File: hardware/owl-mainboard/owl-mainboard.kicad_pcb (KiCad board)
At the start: 4 copper layers, 61.8 x 79.8 mm, 106 parts, among them J101 Battery +, NTC, -, J201 USB-C, J202 EXP: GND, 3V3, A, B, J301 AMOLED FPC, J302 LRA, J303 DOCK: GND, VBUS, DET, GND, SW201 Ear left, SW202 Ear right, SW203 Beak, U101 BQ24073RGTR, U102 MAX17048G+T10, U103 TPS63802DLAR, U104 TPS22917DBVR, U201 ESP32-S3-WROOM-1-N16R8, U202 USBLC6-2SC6, U301 DRV2605LDGSR, U302 TMAG5273A2QDBVR, U303 LIS2DW12TR, U304 OPT3001DNPR, Y201 32.768kHz 12.5pF

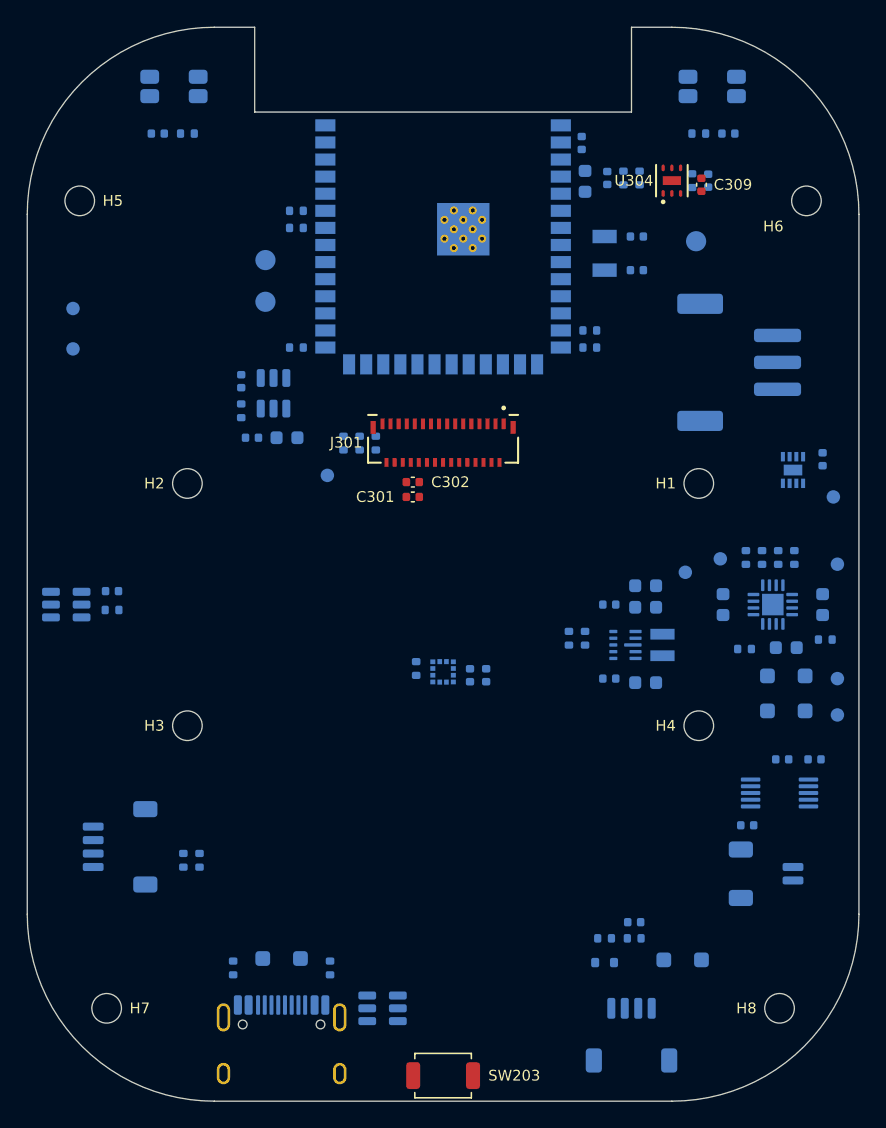
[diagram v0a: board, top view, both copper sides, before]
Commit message: fix(hardware): straighten the USB pair, move C304 and C106 to their pins, put the holes on the front
R203 and R204 stand below U201 pins 14 and 13 with their connector pads at the bottom, and U202
turns to 180 so D+ runs above D- on both sides: the pair goes from J201 through U202 to U201
without crossing (0 crossing airwires). C304 spans DRV2605L VDD pin 10 and GND pin 8, C106 sits
at TPS63802 VIN pin 10 with C105 behind it, and L101's courtyard leaves the battery zone (R44).
H1 to H8 are front in design.toml, as on the board (a bare hole has no side), and the side test
covers them. mark_j101 removes only its own pin 1 dot. R102 3.6k synced from the schematic.
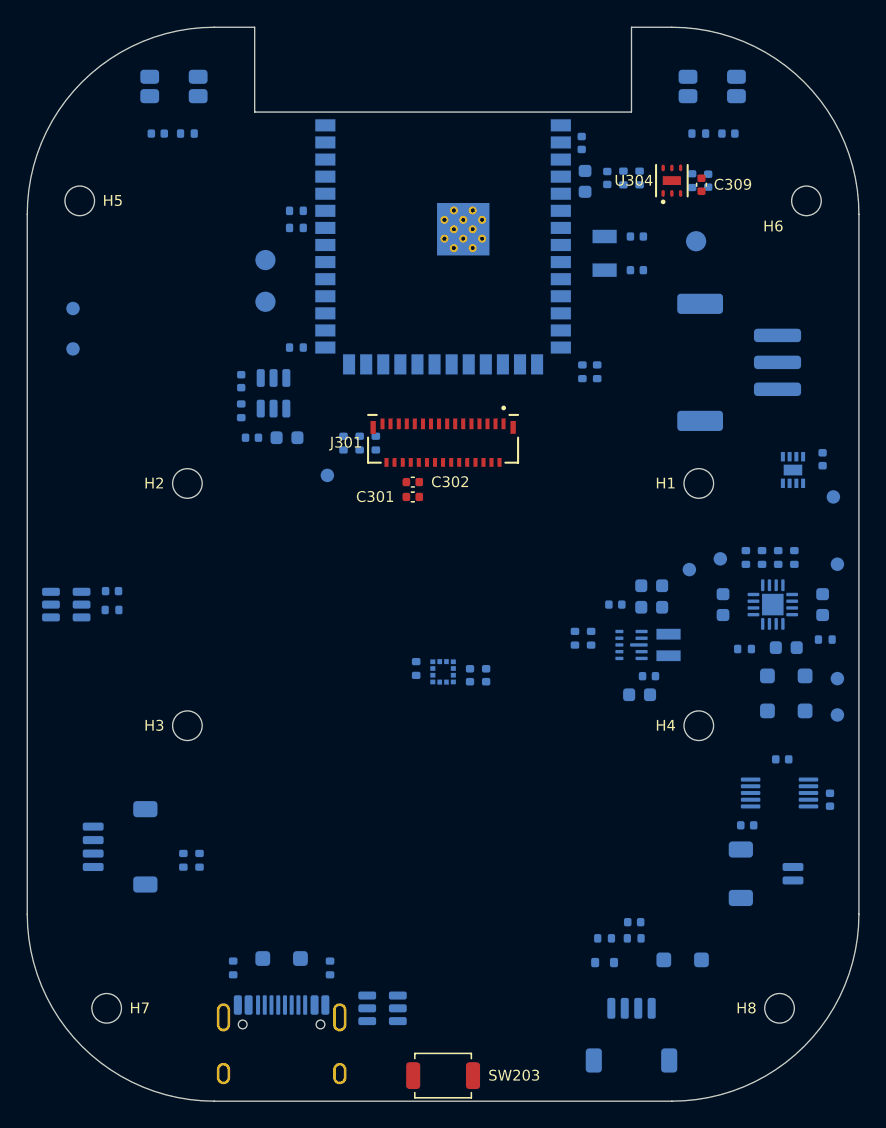
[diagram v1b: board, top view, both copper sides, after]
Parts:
- R102: value 3.3k -> 3.6k
- moved C304 3.21 mm to (128.8, 114.5), turned to 90 degrees
- moved R204 3.12 mm to (111.5, 82.7), turned to 90 degrees
- moved C106 2.96 mm to (115.3, 105.3)
- moved R203 1.88 mm to (110.3, 82.7), turned to 90 degrees
- moved C105 1.01 mm to (114.6, 106.7)
- moved C107 0.45 mm to (115.5, 100.2)
- moved C108 0.45 mm to (115.5, 98.6)
- moved C109 0.45 mm to (112.8, 100.0)
- moved L101 0.45 mm to (116.8, 103.0)
- moved R107 0.45 mm to (111.0, 102.5)
- moved R108 0.45 mm to (109.8, 102.5)
- moved U103 0.45 mm to (114.0, 103.0)
- moved TP104 0.36 mm to (118.3, 97.4)
- turned U202 to 180 degrees

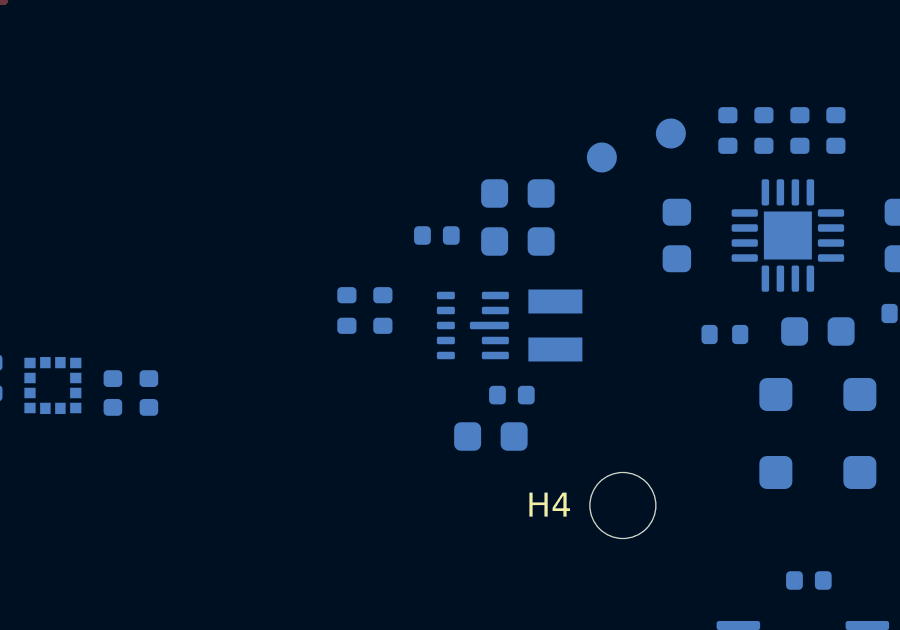
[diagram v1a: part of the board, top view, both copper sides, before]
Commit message: feat(hardware): route the TPS63802 power loop
tools/hw/hw_route.py draws the hand-routed groups as locked B.Cu tracks. The TPS63802 group: L1
and L2 at 0.5 mm straight into L101 (necked to 0.3 mm at the 0.5 mm pitch pins, entering the
inductor pads clear of its no-track area), VIN from pin 10 through C106 to C105 at 0.5 mm, EN to
VIN below the package, VOUT from pin 6 through C107 to C108 at 0.5 mm, C109 and the top of the
feedback divider from C107, FB from pin 4 to R107 and R108 on the side away from L1 and L2 (R107
turned so its FB pad faces R108), GND pins 2, 3 and 8 joined between the pad rows. GND vias and
the In1 tie come with the planes. DRC: no new violation type, 272 to 259 unconnected.
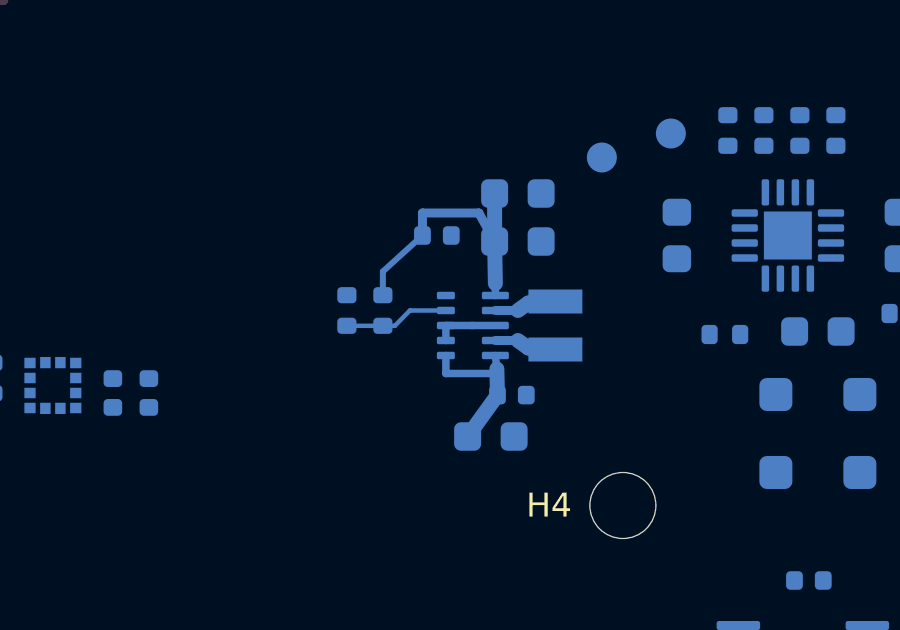
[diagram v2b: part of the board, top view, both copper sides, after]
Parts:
- turned R107 to -90 degrees
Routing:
- net +3V3: track 0.00 -> 9.69 mm
- net VSYS: track 0.00 -> 5.32 mm
- net TPS_FB: track 0.00 -> 3.51 mm
- net TPS_L2: track 0.00 -> 1.83 mm
- net TPS_L1: track 0.00 -> 1.83 mm
- net GND: track 0.00 -> 1.40 mm
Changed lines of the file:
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@@
 	(footprint "Resistor_SMD:R_0402_1005Metric"
 		(layer "B.Cu")
-		(at 111 102.5 90)
+		(at 111 102.5 -90)
 		(descr "Resistor SMD 0402 (1005 Metric), square (rectangular) end terminal, IPC-7351 nominal, (Body size source: IPC-SM-782 page 72, https://www.pcb-3d.com/wordpress/wp-content/uploads/ipc-sm-782a_amendment_1_and_2.pdf)")
 		(tags "resistor")
@@
 		)
 		(property "Value" "560k"
-			(at 0 -1.17 270)
+			(at 0 -1.17 90)
 			(layer "B.Fab")
 			(effects
@@
 		)
 		(property "Datasheet" ""
-			(at 0 0 270)
+			(at 0 0 90)
 			(layer "B.Fab")
 			(hide yes)
@@
 		)
 		(property "Description" "Resistor"
-			(at 0 0 270)
+			(at 0 0 90)
 			(layer "B.Fab")
 			(hide yes)
@@
 		)
 		(property "KiLib_Generator" "SMD_2terminal_chip_molded"
-			(at 0 0 270)
+			(at 0 0 90)
 			(layer "B.SilkS")
 			(hide yes)
@@
 		)
 		(property "LCSC Part #" "C132339"
-			(at 0 0 270)
+			(at 0 0 90)
 			(layer "B.SilkS")
 			(hide yes)
@@
 		)
 		(property "MPN" "0402WGF5603TCE"
-			(at 0 0 270)
+			(at 0 0 90)
 			(layer "B.SilkS")
 			(hide yes)
@@
 		)
 		(property "Manufacturer" "UNI-ROYAL"
-			(at 0 0 270)
+			(at 0 0 90)
 			(layer "B.SilkS")
 			(hide yes)
@@
 		(duplicate_pad_numbers_are_jumpers no)
 		(fp_line
-			(start -0.153641 -0.38)
-			(end 0.153641 -0.38)
+			(start -0.153641 0.38)
+			(end 0.153641 0.38)
 			(stroke
 				(width 0.12)
@@
 		)
 		(fp_line
-			(start -0.153641 0.38)
-			(end 0.153641 0.38)
+			(start -0.153641 -0.38)
+			(end 0.153641 -0.38)
 			(stroke
 				(width 0.12)
@@
 		)
 		(fp_text user "${REFERENCE}"
-			(at 0 0 270)
+			(at 0 0 90)
 			(layer "B.Fab")
 			(effects
@@
 		)
 		(pad "1" smd roundrect
-			(at -0.51 0 90)
+			(at -0.51 0 270)
 			(size 0.54 0.64)
 			(layers "B.Cu" "B.Mask" "B.Paste")
@@
 		)
 		(pad "2" smd roundrect
-			(at 0.51 0 90)
+			(at 0.51 0 270)
 			(size 0.54 0.64)
 			(layers "B.Cu" "B.Mask" "B.Paste")
@@
 		)
 	)
+	(segment
+		(start 113.1 103)
+		(end 114 103)
+		(width 0.25)
+		(locked yes)
+		(layer "B.Cu")
+		(net "GND")
+	)
+	(segment
+		(start 113.1 103.5)
+		(end 113.1 103)
+		(width 0.25)
+		(locked yes)
+		(layer "B.Cu")
+		(net "GND")
+	)
+	(segment
+		(start 112.32 99.25)
+		(end 112.32 100)
+		(width 0.3)
+		(locked yes)
+		(layer "B.Cu")
+		(net "+3V3")
+	)
+	(segment
+		(start 114.75 101.6)
+		(end 114.725 100.2)
+		(width 0.5)
+		(locked yes)
+		(layer "B.Cu")
+		(net "+3V3")
+	)
+	(segment
+		(start 114.725 100.2)
+		(end 114.725 98.6)
+		(width 0.5)
+		(locked yes)
+		(layer "B.Cu")
+		(net "+3V3")
+	)
+	(segment
+		(start 111 101.2)
+		(end 111 101.99)
+		(width 0.2)
+		(locked yes)
+		(layer "B.Cu")
+		(net "+3V3")
+	)
+	(segment
+		(start 114.725 100.2)
+		(end 114.2 99.25)
+		(width 0.3)
+		(locked yes)
+		(layer "B.Cu")
+		(net "+3V3")
+	)
+	(segment
+		(start 114.75 102)
+		(end 114.75 101.6)
+		(width 0.25)
+		(locked yes)
+		(layer "B.Cu")
+		(net "+3V3")
+	)
+	(segment
+		(start 112.32 100)
+		(end 111 101.2)
+		(width 0.2)
+		(locked yes)
+		(layer "B.Cu")
+		(net "+3V3")
+	)
+	(segment
+		(start 114.2 99.25)
+		(end 112.32 99.25)
+		(width 0.3)
+		(locked yes)
+		(layer "B.Cu")
+		(net "+3V3")
+	)
+	(segment
+		(start 114.75 104)
+		(end 114.8 104.45)
+		(width 0.25)
+		(locked yes)
+		(layer "B.Cu")
+		(net "VSYS")
+	)
+	(segment
+		(start 113.1 104)
+		(end 113.1 104.6)
+		(width 0.25)
+		(locked yes)
+		(layer "B.Cu")
+		(net "VSYS")
+	)
+	(segment
+		(start 114.8 104.45)
+		(end 114.82 105.32)
+		(width 0.5)
+		(locked yes)
+		(layer "B.Cu")
+		(net "VSYS")
+	)
+	(segment
+		(start 113.1 104.6)
+		(end 114.8 104.6)
+		(width 0.25)
+		(locked yes)
+		(layer "B.Cu")
+		(net "VSYS")
+	)
+	(segment
+		(start 114.82 105.32)
+		(end 113.825 106.7)
+		(width 0.5)
+		(locked yes)
+		(layer "B.Cu")
+		(net "VSYS")
+	)
+	(segment
+		(start 111.9 102.5)
+		(end 111.4 103.01)
+		(width 0.15)
+		(locked yes)
+		(layer "B.Cu")
+		(net "TPS_FB")
+	)
+	(segment
+		(start 111.4 103.01)
+		(end 111 103.01)
+		(width 0.15)
+		(locked yes)
+		(layer "B.Cu")
+		(net "TPS_FB")
+	)
+	(segment
+		(start 111 103.01)
+		(end 109.8 103.01)
+		(width 0.15)
+		(locked yes)
+		(layer "B.Cu")
+		(net "TPS_FB")
+	)
+	(segment
+		(start 113.1 102.5)
+		(end 111.9 102.5)
+		(width 0.15)
+		(locked yes)
+		(layer "B.Cu")
+		(net "TPS_FB")
+	)
+	(segment
+		(start 115.5 102.5)
+		(end 115.85 102.25)
+		(width 0.5)
+		(locked yes)
+		(layer "B.Cu")
+		(net "TPS_L2")
+	)
+	(segment
+		(start 115.85 102.25)
+		(end 116.5 102.25)
+		(width 0.5)
+		(locked yes)
+		(layer "B.Cu")
+		(net "TPS_L2")
+	)
+	(segment
+		(start 114.75 102.5)
+		(end 115.5 102.5)
+		(width 0.3)
+		(locked yes)
+		(layer "B.Cu")
+		(net "TPS_L2")
+	)
+	(segment
+		(start 115.5 103.5)
+		(end 115.85 103.75)
+		(width 0.5)
+		(locked yes)
+		(layer "B.Cu")
+		(net "TPS_L1")
+	)
+	(segment
+		(start 115.85 103.75)
+		(end 116.5 103.75)
+		(width 0.5)
+		(locked yes)
+		(layer "B.Cu")
+		(net "TPS_L1")
+	)
+	(segment
+		(start 114.75 103.5)
+		(end 115.5 103.5)
+		(width 0.3)
+		(locked yes)
+		(layer "B.Cu")
+		(net "TPS_L1")
+	)
 	(embedded_fonts no)

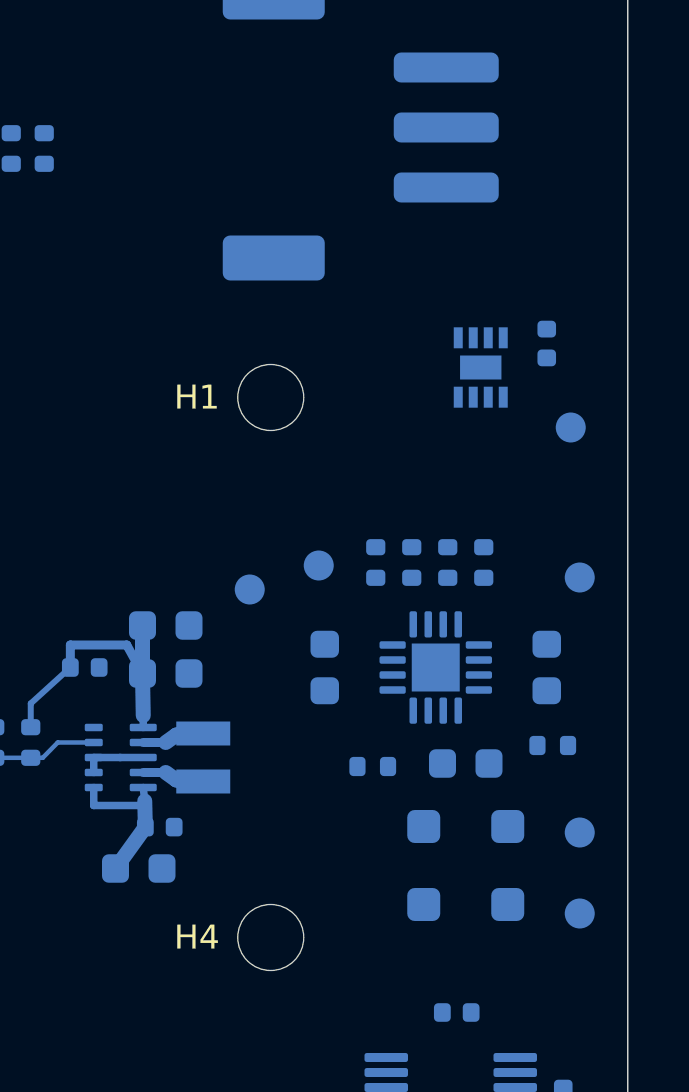
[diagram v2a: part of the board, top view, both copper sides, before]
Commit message: feat(hardware): route the charger power paths and the fuel gauge Kelvin tap
VIN_CHG from BQ24073 pin 13 to C101 and on to the D101 and D102 cathodes, VSYS from pins 10 and
11 to C102 and TP102, VBAT from pins 2 and 3 to C103 and up past TP103, outside the H1 boss
ring, to J101 pin 1: 0.5 mm, necked at the 0.5 mm pitch pins and 0.4 mm between C103 and R103.
The MAX17048 CELL and VDD pins run on their own 0.25 mm trace to J101 pin 1 with C104 at pin 3
(R37). U101's thermal vias wait for the In1 and In2 planes (on their own they are dangling).
DRC: no new violation type, 259 to 246 unconnected.
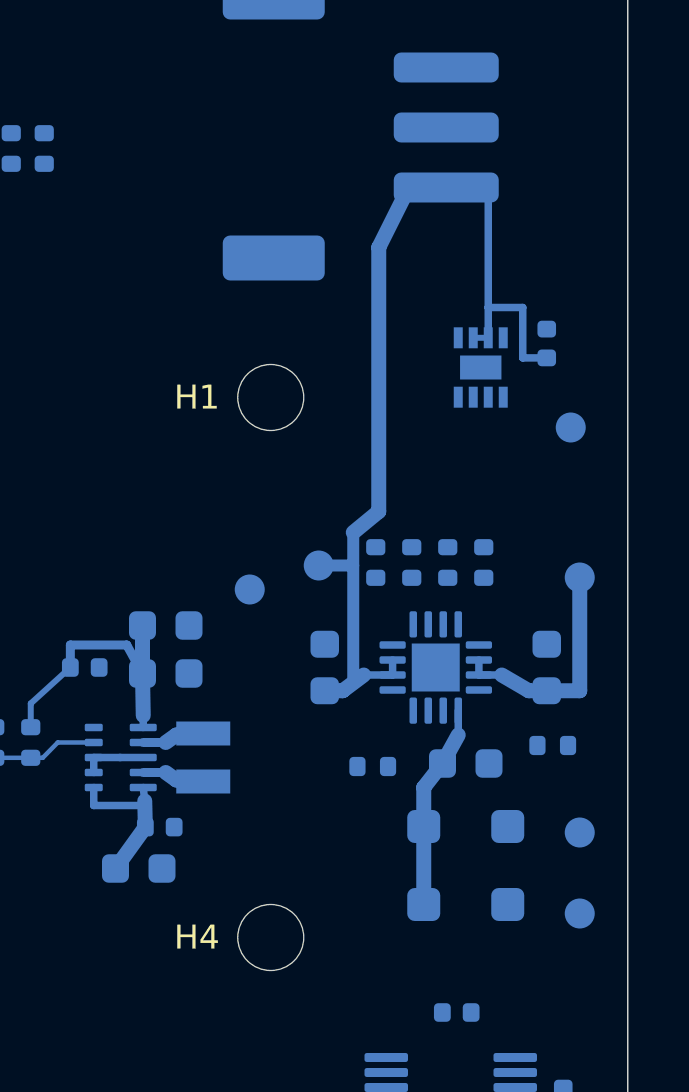
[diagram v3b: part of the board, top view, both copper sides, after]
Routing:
- net VBAT: track 0.00 -> 30.4 mm
- net VSYS: track 5.32 -> 13.1 mm
- net VIN_CHG: track 0.00 -> 6.81 mm
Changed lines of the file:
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@@
+	)
+	(segment
+		(start 122.6 86)
+		(end 123.6 84)
+		(width 0.5)
+		(locked yes)
+		(layer "B.Cu")
+		(net "VBAT")
+	)
+	(segment
+		(start 121.75 100.51)
+		(end 121.75 95.5)
+		(width 0.4)
+		(locked yes)
+		(layer "B.Cu")
+		(net "VBAT")
+	)
+	(segment
+		(start 121.75 95.5)
+		(end 122.6 94.8)
+		(width 0.5)
+		(locked yes)
+		(layer "B.Cu")
+		(net "VBAT")
+	)
+	(segment
+		(start 122.1 100.25)
+		(end 121.4 100.775)
+		(width 0.5)
+		(locked yes)
+		(layer "B.Cu")
+		(net "VBAT")
+	)
+	(segment
+		(start 126.25 88)
+		(end 126.25 89.01)
+		(width 0.25)
+		(locked yes)
+		(layer "B.Cu")
+		(net "VBAT")
+	)
+	(segment
+		(start 126.25 88)
+		(end 127.4 88)
+		(width 0.25)
+		(locked yes)
+		(layer "B.Cu")
+		(net "VBAT")
+	)
+	(segment
+		(start 122.6 94.8)
+		(end 122.6 86)
+		(width 0.5)
+		(locked yes)
+		(layer "B.Cu")
+		(net "VBAT")
+	)
+	(segment
+		(start 126.25 84)
+		(end 126.25 88)
+		(width 0.25)
+		(locked yes)
+		(layer "B.Cu")
+		(net "VBAT")
+	)
+	(segment
+		(start 125.75 89.01)
+		(end 126.25 89.01)
+		(width 0.2)
+		(locked yes)
+		(layer "B.Cu")
+		(net "VBAT")
+	)
+	(segment
+		(start 121.4 100.775)
+		(end 120.8 100.775)
+		(width 0.5)
+		(locked yes)
+		(layer "B.Cu")
+		(net "VBAT")
+	)
+	(segment
+		(start 123.062 99.75)
+		(end 123.062 100.25)
+		(width 0.25)
+		(locked yes)
+		(layer "B.Cu")
+		(net "VBAT")
+	)
+	(segment
+		(start 127.4 88)
+		(end 127.4 89.68)
+		(width 0.25)
+		(locked yes)
+		(layer "B.Cu")
+		(net "VBAT")
+	)
+	(segment
+		(start 120.6 96.6)
+		(end 121.75 96.6)
+		(width 0.4)
+		(locked yes)
+		(layer "B.Cu")
+		(net "VBAT")
+	)
+	(segment
+		(start 123.062 100.25)
+		(end 122.1 100.25)
+		(width 0.25)
+		(locked yes)
+		(layer "B.Cu")
+		(net "VBAT")
+	)
+	(segment
+		(start 127.4 89.68)
+		(end 128.199999 89.68)
+		(width 0.25)
+		(locked yes)
+		(layer "B.Cu")
+		(net "VBAT")
+	)
+	(segment
+		(start 125.25 102.25)
+		(end 124.725 103.2)
+		(width 0.5)
+		(locked yes)
+		(layer "B.Cu")
+		(net "VIN_CHG")
+	)
+	(segment
+		(start 124.725 103.2)
+		(end 124.1 104)
+		(width 0.5)
+		(locked yes)
+		(layer "B.Cu")
+		(net "VIN_CHG")
+	)
+	(segment
+		(start 124.1 104)
+		(end 124.1 105.3)
+		(width 0.5)
+		(locked yes)
+		(layer "B.Cu")
+		(net "VIN_CHG")
+	)
+	(segment
+		(start 124.1 105.3)
+		(end 124.1 107.9)
+		(width 0.5)
+		(locked yes)
+		(layer "B.Cu")
+		(net "VIN_CHG")
+	)
+	(segment
+		(start 125.25 101.438)
+		(end 125.25 102.25)
+		(width 0.25)
+		(locked yes)
+		(layer "B.Cu")
+		(net "VIN_CHG")
 	)
 	(segment
@@
 	)
 	(segment
+		(start 126.7 100.25)
+		(end 127.6 100.775)
+		(width 0.5)
+		(locked yes)
+		(layer "B.Cu")
+		(net "VSYS")
+	)
+	(segment
 		(start 113.1 104)
 		(end 113.1 104.6)
@@
 	)
 	(segment
+		(start 125.938 99.75)
+		(end 125.938 100.25)
+		(width 0.25)
+		(locked yes)
+		(layer "B.Cu")
+		(net "VSYS")
+	)
+	(segment
+		(start 127.6 100.775)
+		(end 128.199999 100.775)
+		(width 0.5)
+		(locked yes)
+		(layer "B.Cu")
+		(net "VSYS")
+	)
+	(segment
+		(start 125.938 100.25)
+		(end 126.7 100.25)
+		(width 0.25)
+		(locked yes)
+		(layer "B.Cu")
+		(net "VSYS")
+	)
+	(segment
 		(start 113.1 104.6)
 		(end 114.8 104.6)
@@
 		(locked yes)
 		(layer "B.Cu")
+		(net "VSYS")
+	)
+	(segment
+		(start 128.199999 100.775)
+		(end 129.3 100.775)
+		(width 0.5)
+		(locked yes)
+		(layer "B.Cu")
+		(net "VSYS")
+	)
+	(segment
+		(start 129.3 100.775)
+		(end 129.3 97)
+		(width 0.5)
+		(locked yes)
+		(layer "B.Cu")
